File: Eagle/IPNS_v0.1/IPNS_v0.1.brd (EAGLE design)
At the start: 100 x 80 mm, 30 parts, among them Q1 16MHz, Q2 32.768 kHz, U1 STM8L152C4_C6TX

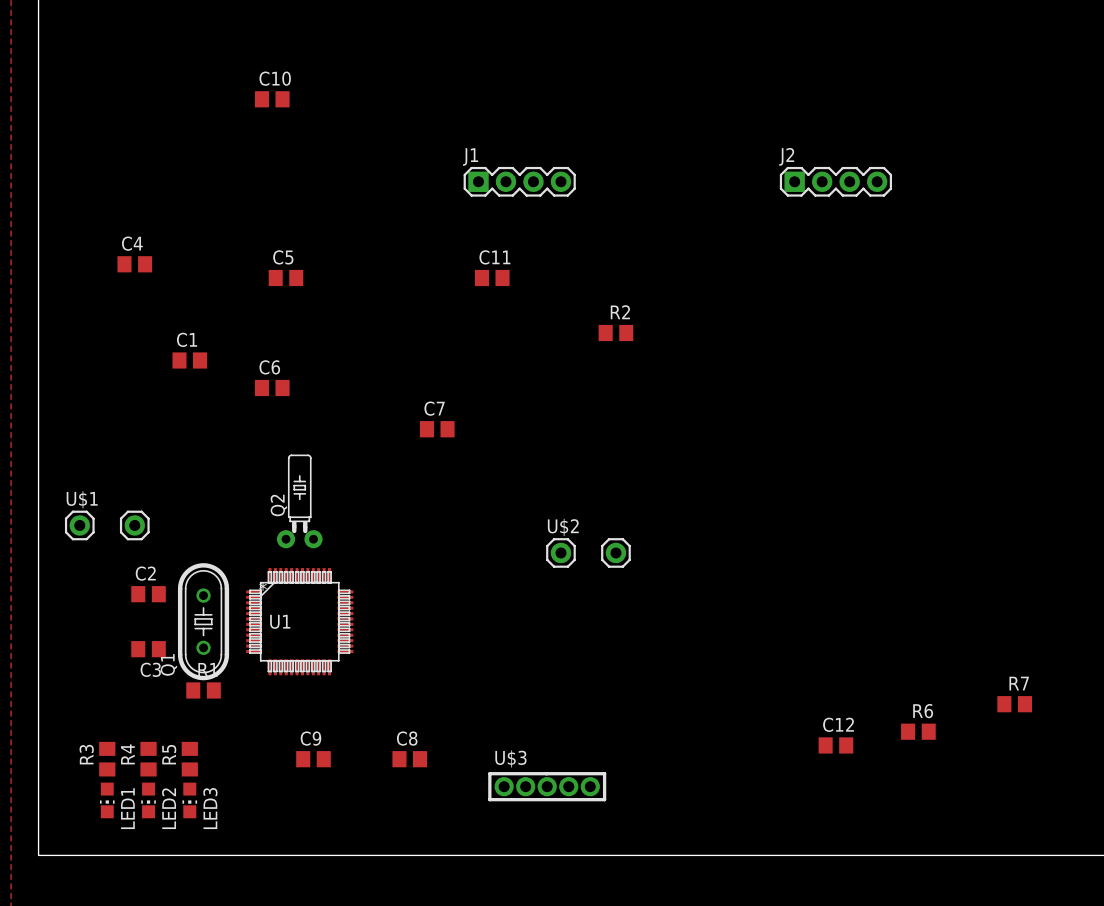
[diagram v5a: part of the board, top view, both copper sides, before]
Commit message: Physical board semi-rearranged
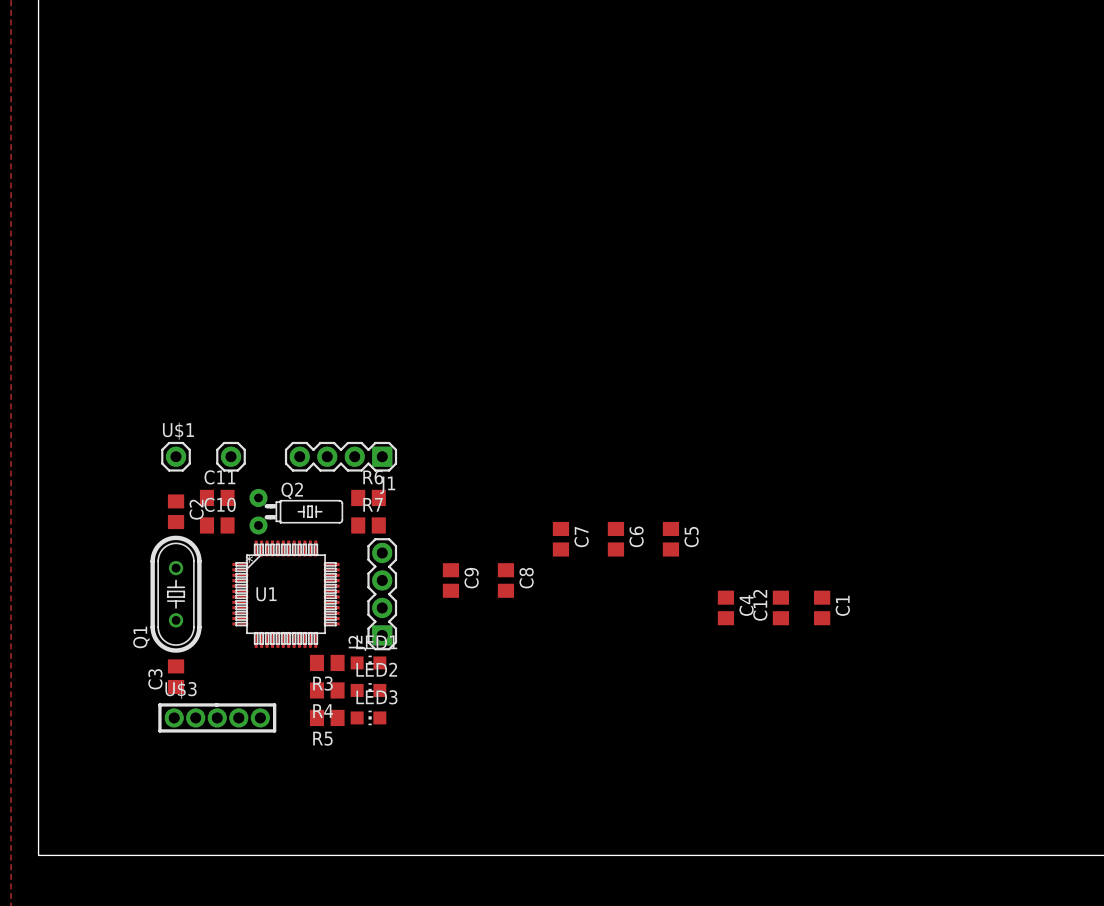
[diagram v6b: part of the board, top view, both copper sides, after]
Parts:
- removed R1, R2: 0, IPNS_Lib_v0.1:R0805
- removed U$2: PUSH-BUTTON, IPNS_Lib_v0.1:PUSH-BUTTON
- moved C4 63.2 mm to (63.5, 22.9), turned to 270 degrees
- moved C1 62.7 mm to (72.4, 22.9), turned to 270 degrees
- moved R7 61.9 mm to (30.5, 30.5)
- moved J2 56.6 mm to (31.8, 20.3), turned to 90 degrees
- moved R6 55.2 mm to (30.5, 33.0)
- moved C5 43.0 mm to (58.4, 29.2), turned to 270 degrees
- moved C10 39.7 mm to (16.5, 30.5)
- moved C6 34.7 mm to (53.3, 29.2), turned to 270 degrees
- moved C11 32.5 mm to (16.5, 33.0)
- moved U$3 31.1 mm to (16.5, 12.7)
- moved LED1 27.3 mm to (30.5, 17.8), turned to 270 degrees
- moved J1 26.9 mm to (31.8, 36.8), turned to 180 degrees
- moved LED2 22.7 mm to (30.5, 15.2), turned to 270 degrees
- moved R3 22.2 mm to (26.7, 17.8), turned to 180 degrees
- moved C9 20.8 mm to (38.1, 25.4), turned to 270 degrees
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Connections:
- removed net N$2: R1.2, U1.4
- removed net N$4: C5.1, C6.1, C7.1, U$2.1
- removed net N$8: R2.2, U1.45
- removed net VDDA: C8.1, C9.1, U$2.3, U1.11, U1.12
- net +3V3: now also C5.1, C6.1, C7.1, C8.1, C9.1, U1.11, U1.12
- net N$14: now also U1.19; no longer U1.48
- net N$15: now also U1.18; no longer U1.47
- net N$16: now also U1.17; no longer U1.19
- net N$3: now also U1.45; no longer R2.1
- net N$5: now also U1.4; no longer R1.1
